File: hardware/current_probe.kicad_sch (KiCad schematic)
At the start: 74 parts, among them J1 SMA, J2 Conn_01x02_Pin, J3 Conn_01x05_Pin, U1 AD8331ARQZ, U2 ADR510ARTZ, U3 ADM7150ARDZ-5.0

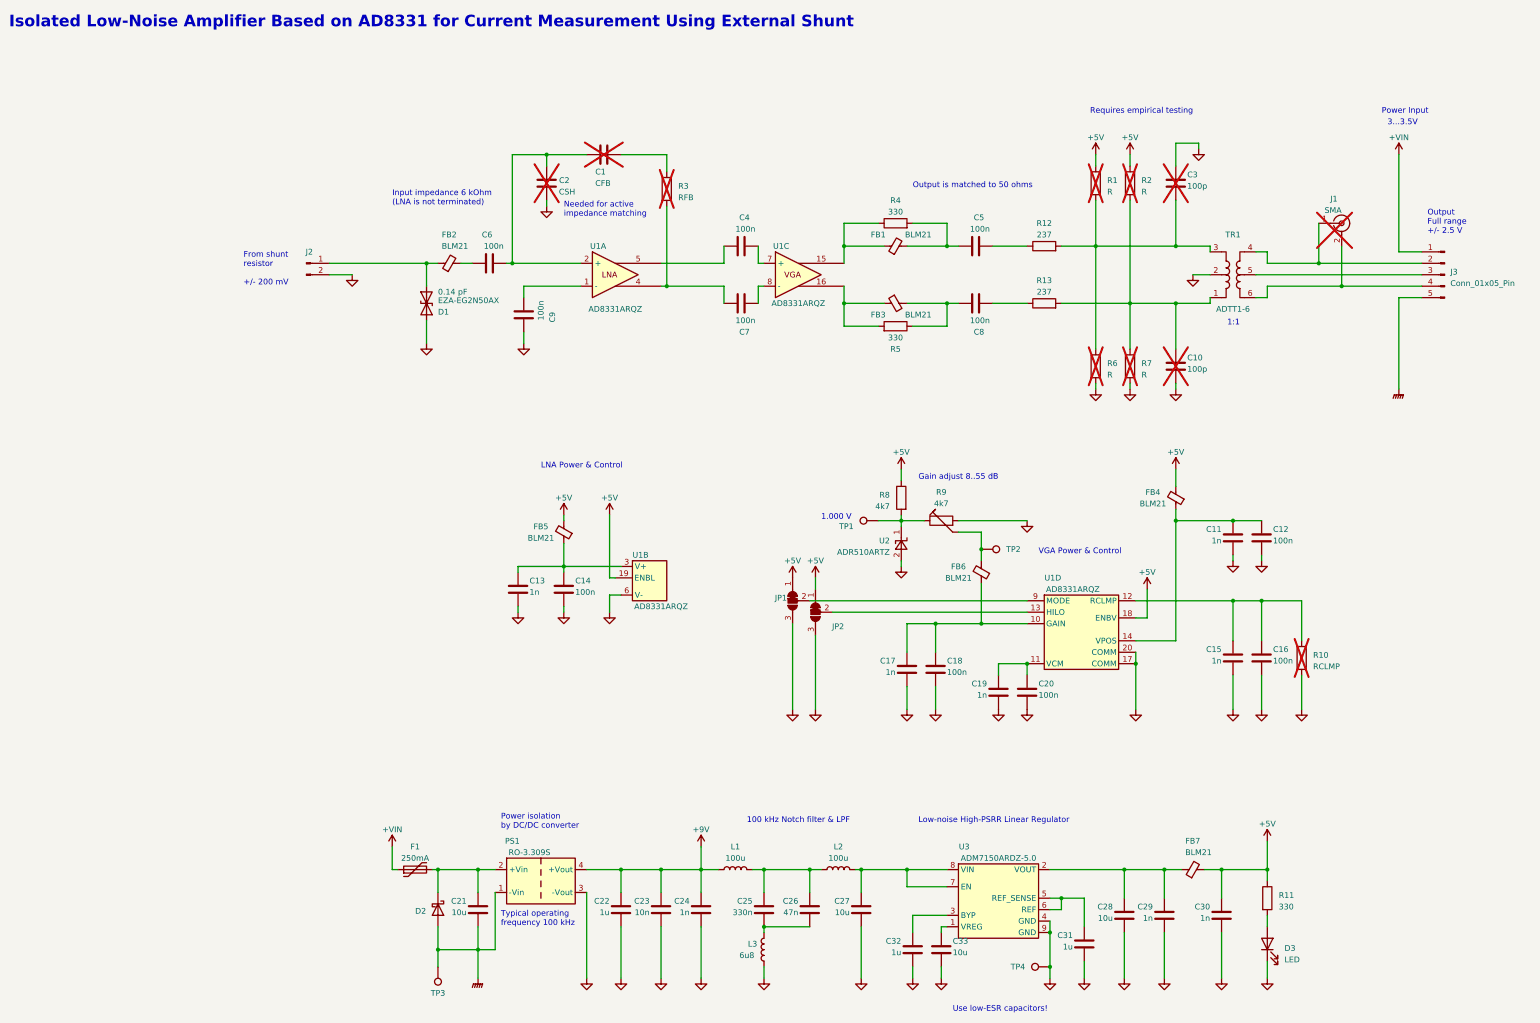
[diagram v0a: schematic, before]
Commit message: Incorporate design review feedback - Enhance routing of input path - Remove voltage reference, used voltage divider instead for gain voltage - Made vias smaller
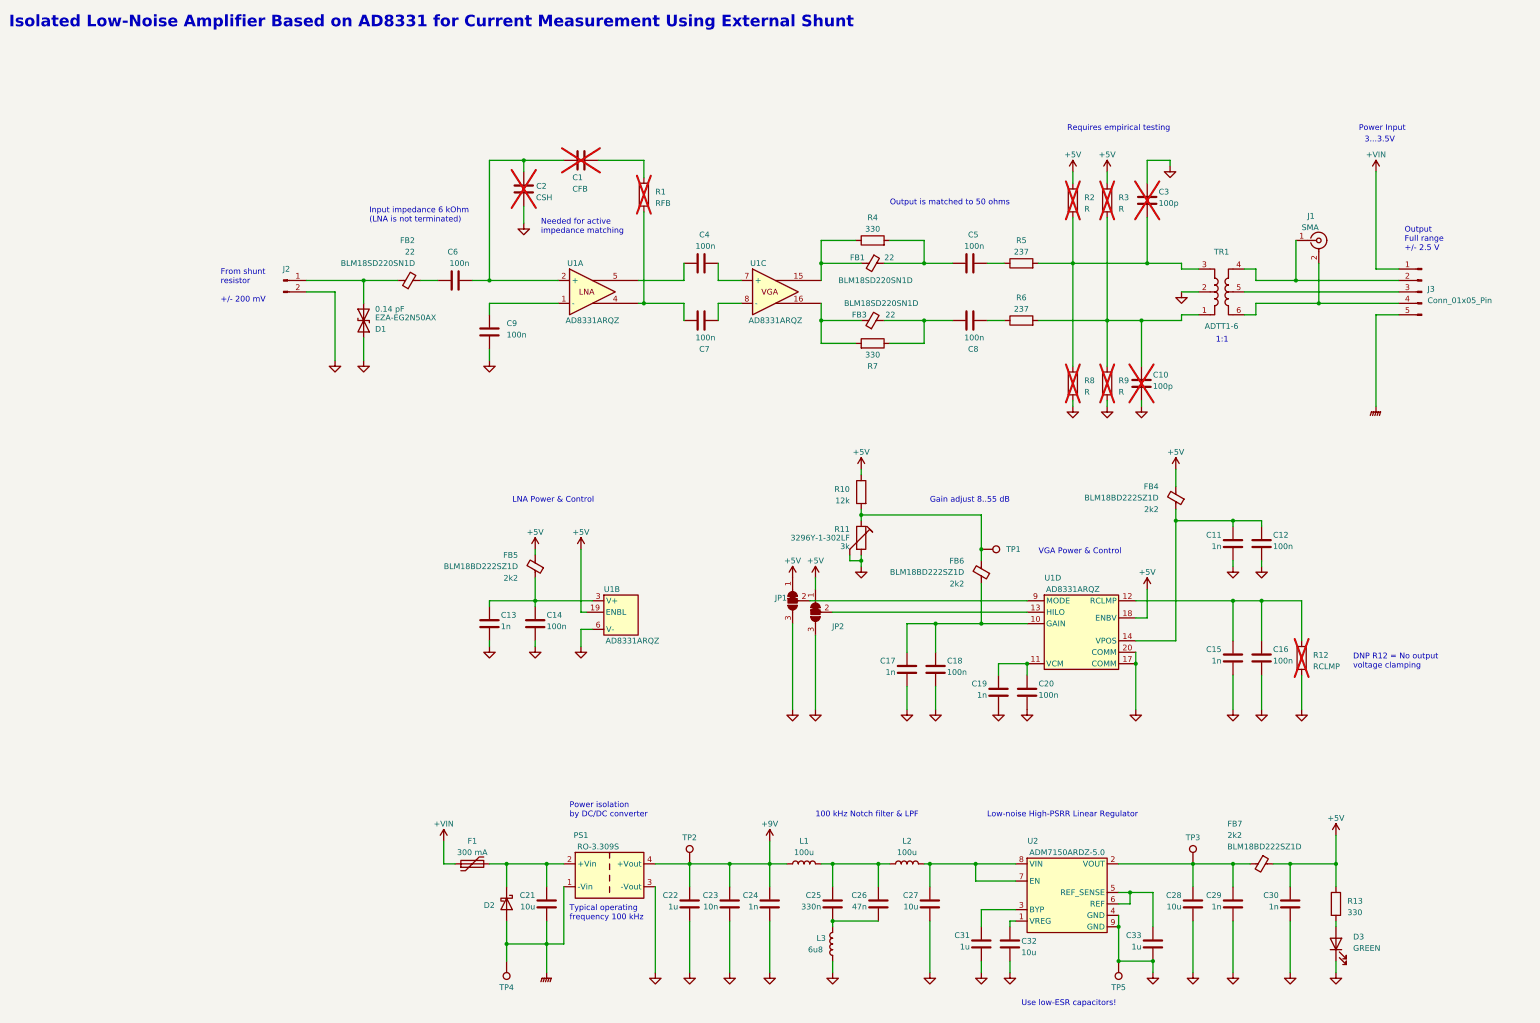
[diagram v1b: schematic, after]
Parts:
- removed TP1: TestPoint, TestPoint:TestPoint_Loop_D1.80mm_Drill1.0mm_Beaded, symbol Connector:TestPoint
- removed U2: ADR510ARTZ, Package_TO_SOT_SMD:SOT-23, symbol Reference_Voltage:LM4040DBZ-3
- added TP2, TP3: TestPoint, TestPoint:TestPoint_Loop_D1.80mm_Drill1.0mm_Beaded, symbol Connector:TestPoint
- D3: value LED -> GREEN
- F1: value 250mA -> 300 mA; Part (none) -> 0805L010/24YR
- FB1, FB2, FB3: value BLM21 -> 22; Part (none) -> BLM18SD220SN1D
- FB4, FB5, FB6, FB7: value BLM21 -> 2k2; Part (none) -> BLM18BD222SZ1D
- J1: Part (none) -> 132289RP; now fitted
- R10: renamed from R8; value 4k7 -> 12k
- R11: renamed from R9; value 4k7 -> 3k; Part (none) -> 3296Y-1-302LF
- TP1: renamed from TP2; footprint TestPoint:TestPoint_Keystone_5000-5004_Miniature -> TestPoint:TestPoint_Loop_D1.80mm_Drill1.0mm_Beaded
- TP4: renamed from TP3; footprint TestPoint:TestPoint_Keystone_5000-5004_Miniature -> TestPoint:TestPoint_Loop_D1.80mm_Drill1.0mm_Beaded
- renumbered C32 to C31, C33 to C32, C31 to C33, R3 to R1, R10 to R12, R11 to R13, R1 to R2, R2 to R3, R12 to R5, R13 to R6, R5 to R7, R6 to R8, R7 to R9, TP4 to TP5, U3 to U2
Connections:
- net +5V: now also FB7.1; no longer FB7.2
- net +9V: now also TP2.1
- net GND: now also R11.3
- net at R10.2, R11.1: now also FB6.2, TP1.1
- net at C5.2, R4.2: now also FB1.1; no longer FB1.2
- net at C28.2, C29.2, U2.2 (VOUT): now also FB7.2, TP3.1; no longer FB7.1
- net at R4.1, U1.15: now also FB1.2; no longer FB1.1
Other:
- note added: "DNP R12 = No output voltage clamping"
- note removed: "1.000 V"
- moved on the sheet: C1, C10, C11, C12, C13, C14, C2, C21, C22, C23, C24, C25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

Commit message: Updated BOM and part numbers
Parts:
- C11, C13, C15, C17, C19, C29, C30: Part (none) -> CL10B102KB8WPNC
- C12, C14, C16, C18, C20, C4, C5, C6, C7, C8, C9: Part (none) -> CL10B104KB8WPNC
- C21, C27, C28, C32: Part (none) -> GCM21BR71A106KE22L
- C22, C31, C33: Part (none) -> GCM21BR71H105MA03L
- C23: Part (none) -> CL10B103KB8WPNC
- C25: Part (none) -> CGA3E3X7R1H334K080AB
- C26: Part (none) -> CGA3E2X7R1H473K080AA
- D1: value EZA-EG2N50AX -> 2.5 pF; Capacitance 0.14 pF -> (none); Part (none) -> GG0603052R542P
- D2: Part (none) -> SK510A-LTP
- D3: Part (none) -> SML-LXT0805GW-TR
- J2: now not fitted
- J3: Part (none) -> 61300511121
- JP1, JP2: now left out of the parts list
- PS1: Part (none) -> RO-3.309S
- R10: Part (none) -> AC0603FR-0712KL
- R13: Part (none) -> RMCF0603FT330R
- R4, R7: value 330 -> 100; Part (none) -> RS73F1JTTD1000B
- R5, R6: Part (none) -> ERJ-PB3B2370V
- TP1, TP2, TP3, TP4, TP5: Part (none) -> 5001
- TR1: value ADTT1-6 -> ADTT1-6+; Part (none) -> ADTT1-6+
- U1: Part (none) -> AD8331ARQZ
- U2: Part (none) -> ADM7150ARDZ-5.0
